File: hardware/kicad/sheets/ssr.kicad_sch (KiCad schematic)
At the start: 31 parts, among them J4 SSR1, J9 SSR2, Q3 AO3400A, Q4 AO3401A, Q5 CJ2310, Q6 CJ2310, Q7 CJ2310, U10 SN74LVC1G123, U8 TLP291, U9 TLP291

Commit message: hardware: coordinate the input clamp with what sits behind it (review item 1 / PCB item 9)
The reviews flagged D8's 48.4 V clamp against the XL1509's 45 V, the
SS34's 40 V and the AO3401A's 30 V, and asked for an envelope rather
than "it is a surge figure". The envelope is now written at F1 in
DESIGN-NOTES: the supply is the in-enclosure HDR-15-24 or its class
(<= 1 A limit) on wiring that stays in the box, and the SMAJ30A's own
table then bounds the rail at 36.8 V + 1.4 ohm x I - 38.1 V at the
supply's 0.91 A limit, 40 V up to F1's 2.3 A, U11's 45 V abs max only
at 5.8 A, 48.4 V only on the 10/1000 us pulse. The sustained,
current-limited case ends with D8 failing short at <= 38 V, which is
the intended outcome.

The TVS stays. The Mean Well sheet gives the HDR-15-24's trim range as
21.6-29 V, not the +-10% (26.4 V) the notes assumed, so an SMAJ28A would
stand off less than the supply can be set to. Q8 is not stressed in a
forward fault (body diode conducts, D11 clamps the gate). The two parts
with no margin at 38 V were the 40 V diodes that see the rail in
reverse, and both change in the same land:

- D7  SS34  -> SS36 (R+O C7420367), 60 V 3 A SMA. VF 0.70 V vs 0.55 V,
  ~1% of buck efficiency at full load.
- D9/D10 B5819W -> 1N4007W (FUXINSEMI C3018540, SOD-123 body), 1 kV
  1 A. With its channel on the freewheel diode stands off the whole
  rail; a standard-recovery rectifier is the right part for a contactor
  coil at the SSR timer's rate. Drawn with Device:D, not the Schottky
  symbol.

Both are Extended where the old parts were Basic; on Standard PCBA,
where this BOM is, the bill is unchanged (49 lines). lcsc_pads.json
carries both land patterns (resid 0.150 / 0.023 mm), the datasheets
are cached and mapped, SS34/B5819W PDFs recorded as retired. The 26.4 V
trim figure is corrected to 29 V in DESIGN-NOTES, the enclosure README
and the bench smoke test; dated status on both review findings and the
10-22 status table. Still named open: the external SSR input at 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
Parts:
- D10, D9: value B5819W -> 1N4007W; symbol Device:D_Schottky -> Device:D; LCSC C8598 -> C3018540; MPN B5819W SL -> 1N4007W; Manufacturer JSCJ -> FUXINSEMI
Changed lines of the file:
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@@
 	)
 	(symbol
-		(lib_id "Device:D_Schottky")
+		(lib_id "Device:D")
 		(at 66.04 153.67 0)
 		(unit 1)
@@
 			)
 		)
-		(property "Value" "B5819W"
+		(property "Value" "1N4007W"
 			(at 62.23 150.49 0)
 			(show_name no)
@@
 			)
 		)
-		(property "Datasheet" "https://datasheet.lcsc.com/datasheet/pdf/4ac2c059be7c462694ab0715ce987a85.pdf?productCode=C8598"
+		(property "Datasheet" "https://datasheet.lcsc.com/datasheet/pdf/a7dbd01177530af63da342fa61873c89.pdf?productCode=C3018540"
 			(at 66.04 153.67 0)
 			(hide yes)
@@
 			)
 		)
-		(property "Description" "Schottky diode"
+		(property "Description" "Diode"
 			(at 66.04 153.67 0)
 			(hide yes)
@@
 			)
 		)
-		(property "MPN" "B5819W SL"
+		(property "MPN" "1N4007W"
 			(at 66.04 153.67 0)
 			(hide yes)
@@
 			)
 		)
-		(property "LCSC" "C8598"
+		(property "LCSC" "C3018540"
 			(at 66.04 153.67 0)
 			(hide yes)
@@
 			)
 		)
-		(property "Manufacturer" "JSCJ"
+		(property "Manufacturer" "FUXINSEMI"
 			(at 66.04 153.67 0)
 			(hide yes)
@@
 	)
 	(symbol
-		(lib_id "Device:D_Schottky")
+		(lib_id "Device:D")
 		(at 66.04 82.55 0)
 		(unit 1)
@@
 			)
 		)
-		(property "Value" "B5819W"
+		(property "Value" "1N4007W"
 			(at 62.23 79.37 0)
 			(show_name no)
@@
 			)
 		)
-		(property "Datasheet" "https://datasheet.lcsc.com/datasheet/pdf/4ac2c059be7c462694ab0715ce987a85.pdf?productCode=C8598"
+		(property "Datasheet" "https://datasheet.lcsc.com/datasheet/pdf/a7dbd01177530af63da342fa61873c89.pdf?productCode=C3018540"
 			(at 66.04 82.55 0)
 			(hide yes)
@@
 			)
 		)
-		(property "Description" "Schottky diode"
+		(property "Description" "Diode"
 			(at 66.04 82.55 0)
 			(hide yes)
@@
 			)
 		)
-		(property "MPN" "B5819W SL"
+		(property "MPN" "1N4007W"
 			(at 66.04 82.55 0)
 			(hide yes)
@@
 			)
 		)
-		(property "LCSC" "C8598"
+		(property "LCSC" "C3018540"
 			(at 66.04 82.55 0)
 			(hide yes)
@@
 			)
 		)
-		(property "Manufacturer" "JSCJ"
+		(property "Manufacturer" "FUXINSEMI"
 			(at 66.04 82.55 0)
 			(hide yes)

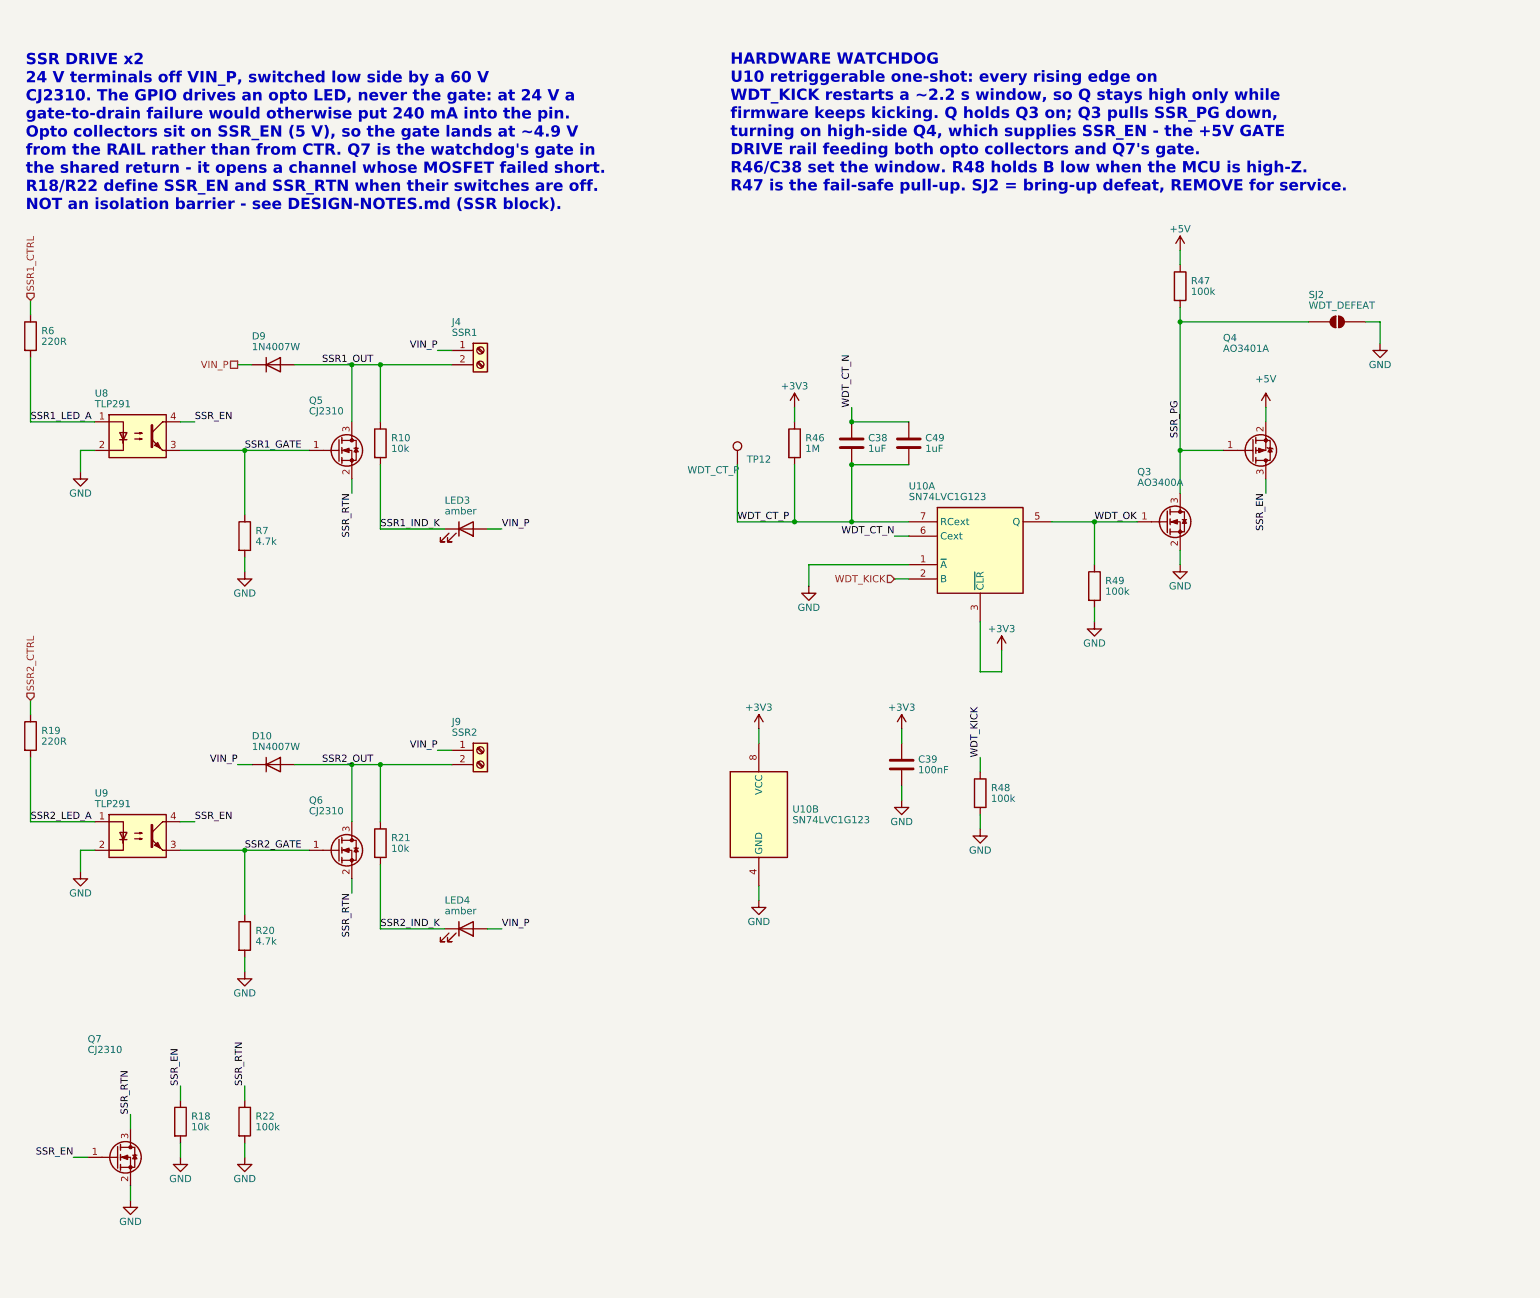
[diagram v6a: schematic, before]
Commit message: hardware: rev B.4 - SSR outputs switch the + side, - pin on GND, watchdog cutoff in the 24 V rail
Schematic review 2026-10-05 item 3 (fab review A1) and item 11, closed by
redesign rather than by documentation.

Rev B.2 kept each SSR terminal's pin 1 on the always-live VIN_P, switched
the return with a CJ2310 per channel and put the watchdog's Q7 in the
shared return. An SSR - lead that found ground - the earthed backplate,
the PSU -, a commoned negative - turned that SSR on with nothing on the
board able to turn it off, and a failed-short channel with the window
expired put -23.7 V on the healthy channel's gate through R22.

Now each terminal's pin 1 (silk OUT) is the drain of a 60 V P-channel
LP2309LT1G (Q5/Q6, LRC C383253) whose source is SSR_24V, and pin 2 (silk
GND) is board ground; the pin order is unchanged, so a loom built to the
B.2/B.3 silk still lands right. The opto (U8/U9) pulls the gate down
through 10k (R69/R70), an 8.2 V BZT52C8V2S gate-source zener (D13/D14)
sets V_SG from the rail rather than from CTR, and 10k (R7/R20, from
4.7k) holds the gate at the source against the opto's 85 C dark current
(0.5 V against a 1 V threshold floor). SSR_24V is VIN_P through Q9, a
third LP2309LT1G that is the watchdog's cutoff: Q7 (the one remaining
CJ2310, gate on SSR_EN) pulls Q9's gate down through R71 (10k), D12
clamps it to 8.2 V and R22 (100k) holds Q9 off otherwise. D9/D10 now
freewheel cathode-on-OUT; LED3/LED4 read OUT to GND through R10/R21.

A - lead on ground is the wiring diagram. A + lead on the chassis is a
short the HDR-15-24's current limit (or F1 on a bigger supply) ends with
the SSR off. A failed-short channel is cut by Q9 when the e-stop blocks
the kick - the coverage B.1 had. With Q9 open nothing pulls SSR_24V, so
item 11's gate stress cannot occur. B.2 rejected a high-side cutoff for
want of a fee-free 60 V P-FET; on Standard PCBA every line pays the same
$1.53, and C383253 (165k in stock) is the part that objection said did
not exist. One new 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
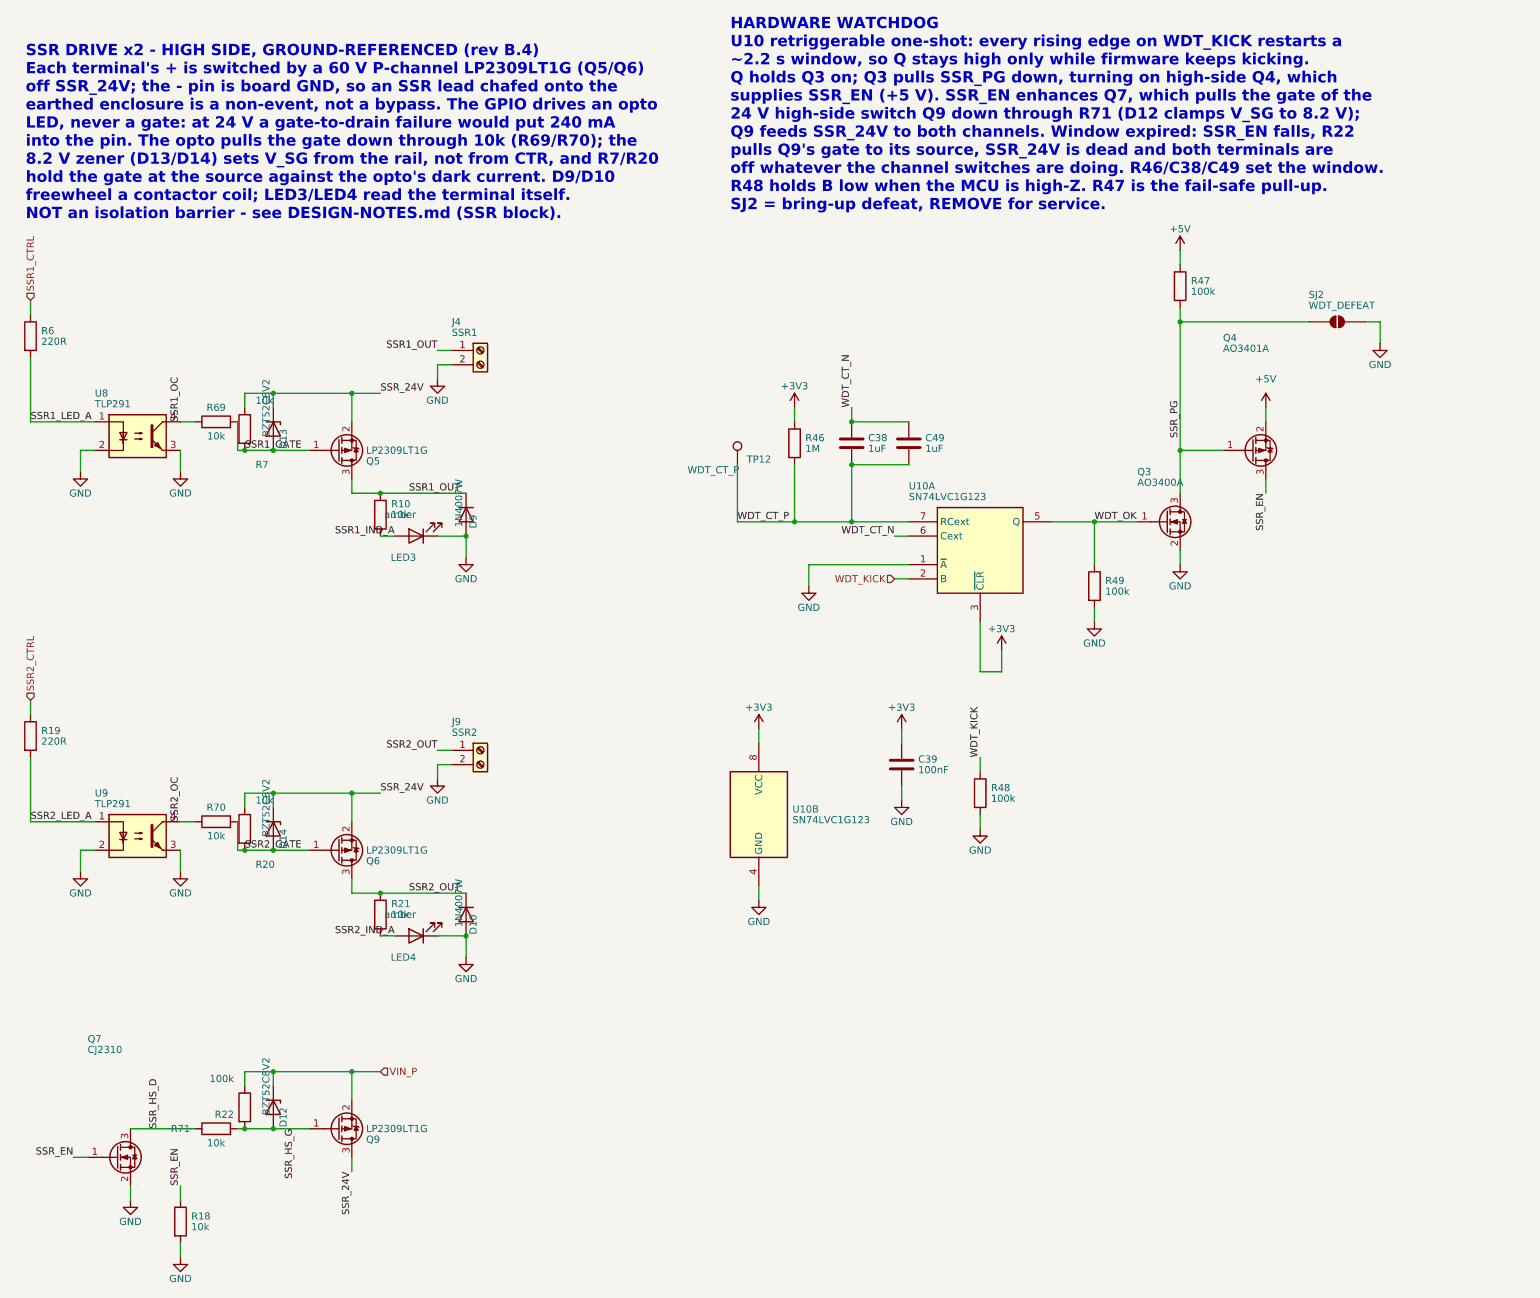
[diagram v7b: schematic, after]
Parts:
- added D12, D13, D14: BZT52C8V2, Diode_SMD:D_SOD-323, symbol Device:D_Zener
- added Q9: LP2309LT1G, Package_TO_SOT_SMD:SOT-23, symbol bisque:LP2309LT1G
- added R69, R70, R71: 10k, Resistor_SMD:R_0805_2012Metric, symbol Device:R
- Q5, Q6: value CJ2310 -> LP2309LT1G; symbol bisque:CJ2310 -> bisque:LP2309LT1G; LCSC C75882 -> C383253; MPN CJ2310 -> LP2309LT1G; Manufacturer JSCJ -> LRC
- R20, R7: value 4.7k -> 10k; LCSC C17673 -> C17414; MPN 0805W8F4701T5E -> 0805W8F1002T5E
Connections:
- net GND: now also D10.2 (A), D9.2 (A), J4.2 (Pin_2), J9.2 (Pin_2), LED3.1 (K), LED4.1 (K), U8.3, U9.3; no longer R20.2, R22.2, R7.2
- net SSR1_GATE: now also R7.2, D13.2 (A), R69.2; no longer R7.1, U8.3
- net SSR1_OUT: now also D9.1 (K), J4.1 (Pin_1); no longer D9.2 (A), J4.2 (Pin_2)
- net SSR2_GATE: now also R20.2, D14.2 (A), R70.2; no longer R20.1, U9.3
- net SSR2_OUT: now also D10.1 (K), J9.1 (Pin_1); no longer D10.2 (A), J9.2 (Pin_2)
- net SSR_EN: no longer U8.4, U9.4
- net VIN_P: now also R22.1, D12.1 (K), Q9.2 (S); no longer D10.1 (K), D9.1 (K), J4.1 (Pin_1), J9.1 (Pin_1), LED3.2 (A), LED4.2 (A)
- net SSR1_IND_K renamed SSR1_IND_A
- net SSR1_IND_A: now also LED3.2 (A); no longer LED3.1 (K)
- net SSR2_IND_K renamed SSR2_IND_A
- net SSR2_IND_A: now also LED4.2 (A); no longer LED4.1 (K)
- net SSR_RTN renamed SSR_24V
- net SSR_24V: now also R20.1, R7.1, D13.1 (K), D14.1 (K), Q9.3 (D); no longer Q7.3 (D), R22.1
- new net SSR1_OC: R69.1, U8.4
- new net SSR2_OC: R70.1, U9.4
- new net SSR_HS_D: Q7.3 (D), R71.1
- new net SSR_HS_G: D12.2 (A), Q9.1 (G), R22.2, R71.2
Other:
- note added: "HARDWARE WATCHDOG U10 retriggerable one-shot: every rising edge on WDT_KICK restarts a ~2.2 s window, so Q stays high only while firmware keeps kicking. Q holds Q3 on; Q3 pulls SSR_PG down, turning on high-side Q4, which supplies SSR_EN (+5 V). SSR_EN enhances Q7, which pulls the gate of the 24 V high-side switch Q9 down through R71 (D12 clamps V_SG to 8.2 V); Q9 feeds SSR_24V to both channels. W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"
- note added: "SSR DRIVE x2 - HIGH SIDE, GROUND-REFERENCED (rev B.4) Each terminal's + is switched by a 60 V P-channel LP2309LT1G (Q5/Q6) off SSR_24V; the - pin is board GND, so an SSR lead chafed onto the earthed enclosure is a non-event, not a bypass. The GPIO drives an opto LED, never a gate: at 24 V a gate-to-drain failure would put 240 mA into the pin. The opto pulls the gate down through 10k (R69/R70); th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"
- note removed: "HARDWARE WATCHDOG U10 retriggerable one-shot: every rising edge on WDT_KICK restarts a ~2.2 s window, so Q stays high only while firmware keeps kicking. Q holds Q3 on; Q3 pulls SSR_PG down, turning on high-side Q4, which supplies SSR_EN - the +5V GATE DRIVE rail feeding both opto collectors and Q7's gate. R46/C38 set the window. R48 holds B low when the MCU is high-Z. R47 is the fail-safe pull-up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"
- note removed: "SSR DRIVE x2 24 V terminals off VIN_P, switched low side by a 60 V CJ2310. The GPIO drives an opto LED, never the gate: at 24 V a gate-to-drain failure would otherwise put 240 mA into the pin. Opto collectors sit on SSR_EN (5 V), so the gate lands at ~4.9 V from the RAIL rather than from CTR. Q7 is the watchdog's gate in the shared return - it opens a channel whose MOSFET failed short. R18/R22 de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"
- moved on the sheet: D10, D9, LED3, LED4, R10, R18, R20, R21, R22, R7

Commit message: hardware: BOM from the schematic, JLCPCB fits every part
BOM.csv is now kicad-cli's export of the schematic itself (make pcb-fab),
so every symbol not marked "Exclude from BOM" is on it; gen_jlc reads the
same flags instead of a hand-kept NOT_ASSEMBLED/HAND_SOLDER table.

JLCPCB assembly of the 12 through-hole parts plus LED1 costs ~$22 an order
against ~$110 for partial assembly and a Mouser order, so they are no
longer hand-fitted. Their Assembly field reads "Optional hand solder - JLC
assembles; untick at JLC to fit by hand"; setting it back to "HAND SOLDER"
makes a part hand-fitted again. JLC_PLACEMENT gains fitted corrections for
the six new LCSC parts (J7 needs 180 deg).

LED1 moves to the in-stock WS2812B-V5/W (C2874885): same pinout, and its
VIH of 0.63*VDD (~2.6 V at VLED) is below the old part's 2.7 V.
mouser-order.csv now holds only the mating housings and crimps.

Co-Authored-By: Claude Opus 5.5 <noreply@anthropic.com>
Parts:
- J4, J9: Assembly (none) -> Optional hand solder - JLC assembles; untick at JLC to fit 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
- SJ2, TP12: now left out of the parts list
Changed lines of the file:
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@@
 		(unit 1)
 		(exclude_from_sim no)
-		(in_bom yes)
+		(in_bom no)
 		(on_board yes)
 		(dnp no)
@@
 		(unit 1)
 		(exclude_from_sim no)
-		(in_bom yes)
+		(in_bom no)
 		(on_board yes)
 		(dnp no)
@@
 			)
 		)
-	)
+		(property "Assembly" "Optional hand solder - JLC assembles; untick at JLC to fit by hand"
+			(at 102.87 151.13 0)
+			(hide yes)
+			(effects
+				(font
+					(size 1.27 1.27)
+				)
+			)
+		))
 	(symbol
 		(lib_id "Device:R")
@@
 			)
 		)
-	)
+		(property "Assembly" "Optional hand solder - JLC assembles; untick at JLC to fit by hand"
+			(at 102.87 80.01 0)
+			(hide yes)
+			(effects
+				(font
+					(size 1.27 1.27)
+				)
+			)
+		))
 	(symbol
 		(lib_id "Device:R")
